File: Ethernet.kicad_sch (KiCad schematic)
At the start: 1 part, among them U1 rv1126/rv1109

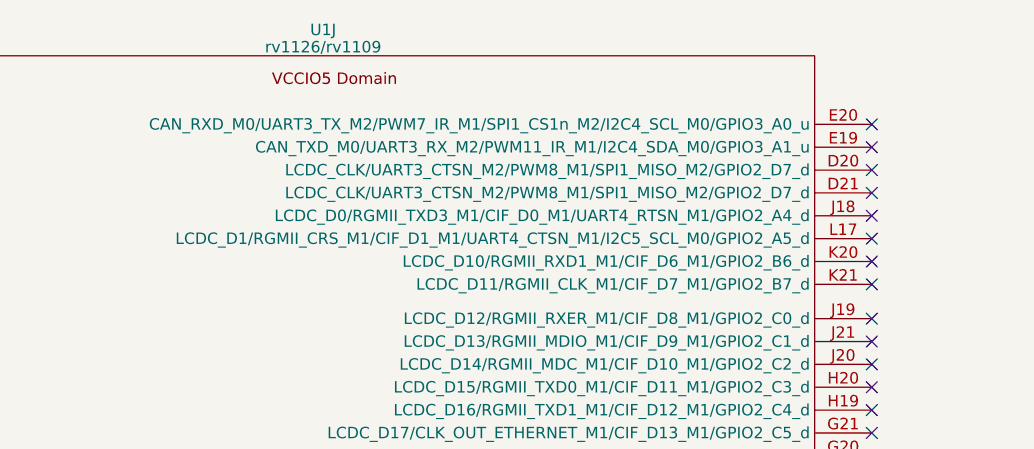
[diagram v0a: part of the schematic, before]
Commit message: fix some ERCs
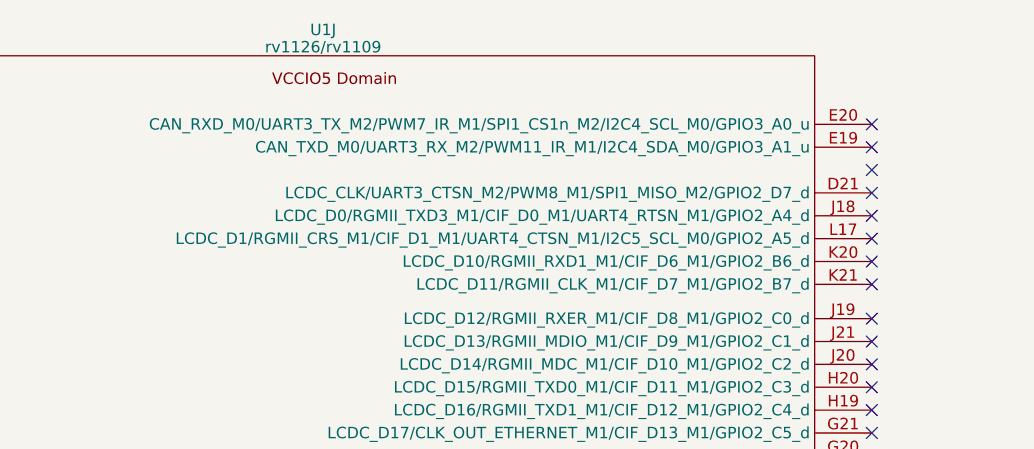
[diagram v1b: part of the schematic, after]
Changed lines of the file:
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@@
     (pin "Y21")
     (pin "C21")
-    (pin "D20")
     (pin "D21")
     (pin "E19")
@@
     (pin "Y21")
     (pin "C21")
-    (pin "D20")
     (pin "D21")
     (pin "E19")

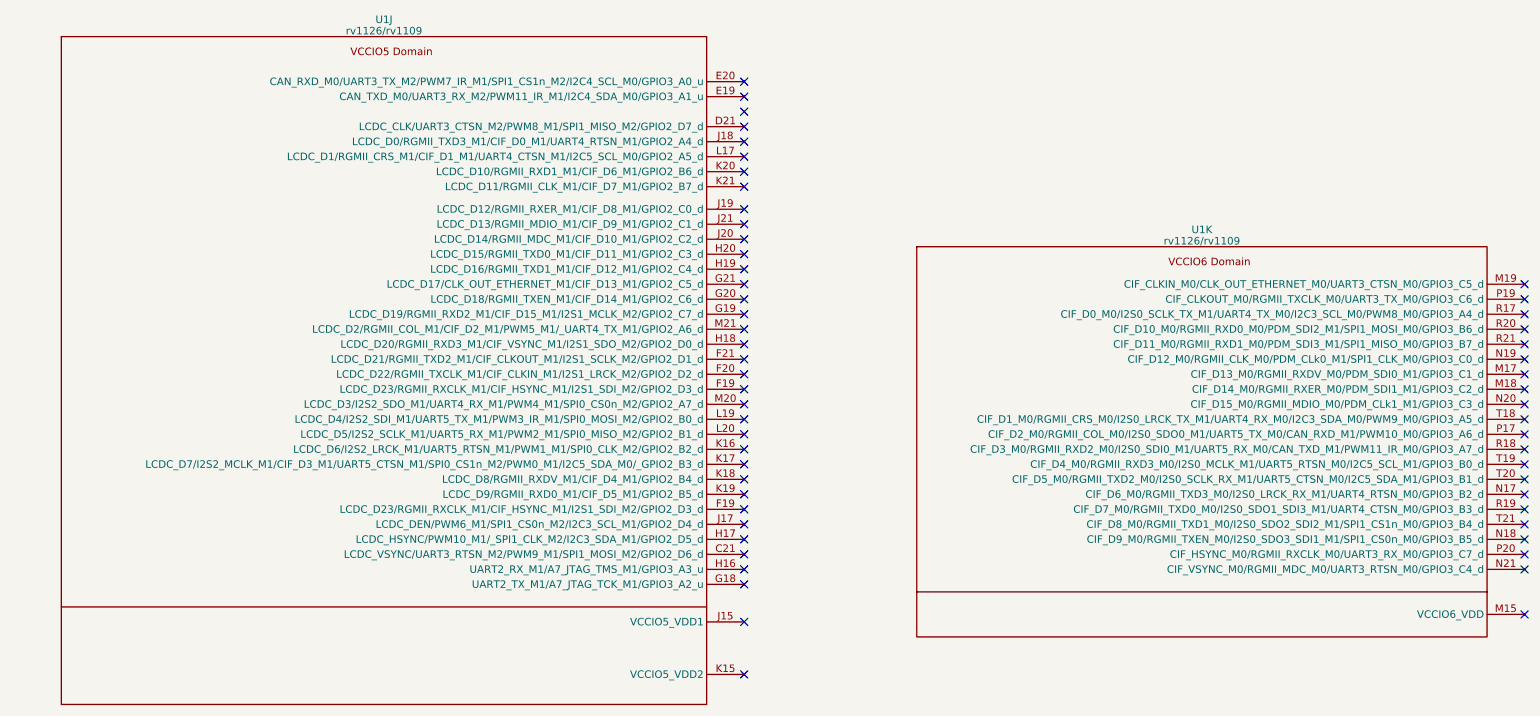
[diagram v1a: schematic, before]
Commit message: fix ERC
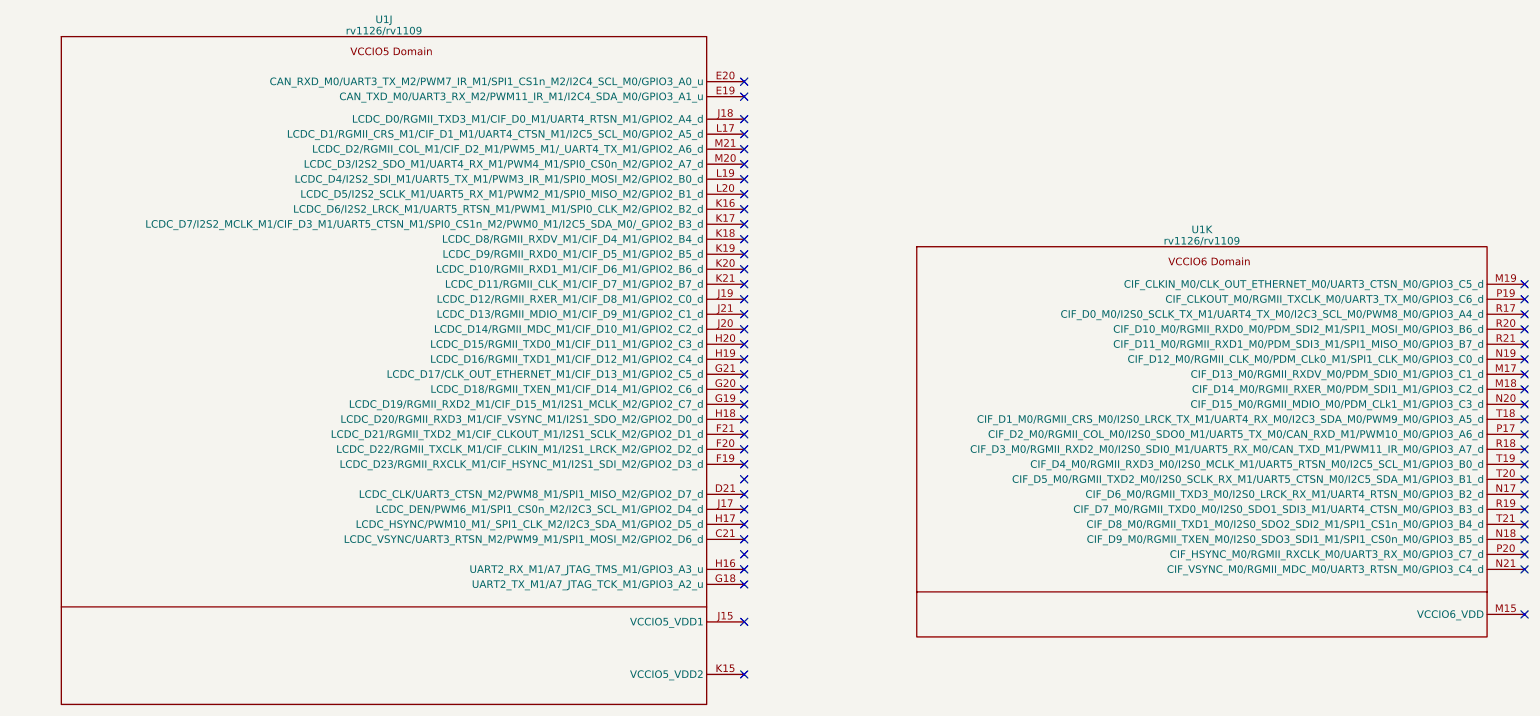
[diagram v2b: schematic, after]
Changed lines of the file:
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@@
   (no_connect (at 144.78 69.85))
   (no_connect (at 144.78 87.63))
+  (no_connect (at 144.78 41.91))
   (no_connect (at 144.78 74.93))
   (no_connect (at 276.86 80.01))
@@
   (no_connect (at 144.78 115.57))
   (no_connect (at 144.78 35.56))
-  (no_connect (at 144.78 48.26))
+  (no_connect (at 144.78 49.53))
   (no_connect (at 144.78 92.71))
   (no_connect (at 144.78 120.65))
@@
   (no_connect (at 144.78 100.33))
   (no_connect (at 276.86 125.73))
-  (no_connect (at 144.78 45.72))
-  (no_connect (at 144.78 53.34))
+  (no_connect (at 144.78 46.99))
+  (no_connect (at 144.78 54.61))
   (no_connect (at 144.78 57.15))
   (no_connect (at 144.78 90.17))
@@
   (no_connect (at 144.78 113.03))
   (no_connect (at 144.78 110.49))
-  (no_connect (at 144.78 43.18))
+  (no_connect (at 144.78 44.45))
   (no_connect (at 276.86 82.55))
   (no_connect (at 276.86 90.17))
-  (no_connect (at 144.78 50.8))
+  (no_connect (at 144.78 52.07))
   (no_connect (at 276.86 102.87))
   (no_connect (at 144.78 38.1))
   (no_connect (at 144.78 127))
-  (no_connect (at 144.78 40.64))
   (no_connect (at 276.86 105.41))
   (no_connect (at 144.78 62.23))
@@
     )
   )
-  (symbol (lib_id "CPU_Rockchip:rv1126_rv1109") (at 83.82 57.15 0) (unit 10)
+  (symbol (lib_name "rv1126_rv1109_1") (lib_id "CPU_Rockchip:rv1126_rv1109") (at 83.82 57.15 0) (unit 10)
     (in_bom yes) (on_board yes) (dnp no) (fields_autoplaced)
     (property "Reference" "U1" (at 83.82 25.0571 0)
@@
     (pin "E20")
     (pin "F19")
-    (pin "F19")
     (pin "F20")

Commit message: fix warnings
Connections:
- no-connect marks 57 -> 55
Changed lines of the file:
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@@
   (no_connect (at 144.78 107.95))
   (no_connect (at 144.78 95.25))
-  (no_connect (at 144.78 115.57))
   (no_connect (at 144.78 35.56))
   (no_connect (at 144.78 49.53))
@@
   (no_connect (at 276.86 77.47))
   (no_connect (at 276.86 69.85))
-  (no_connect (at 144.78 102.87))
   (no_connect (at 276.86 118.11))
   (no_connect (at 276.86 113.03))

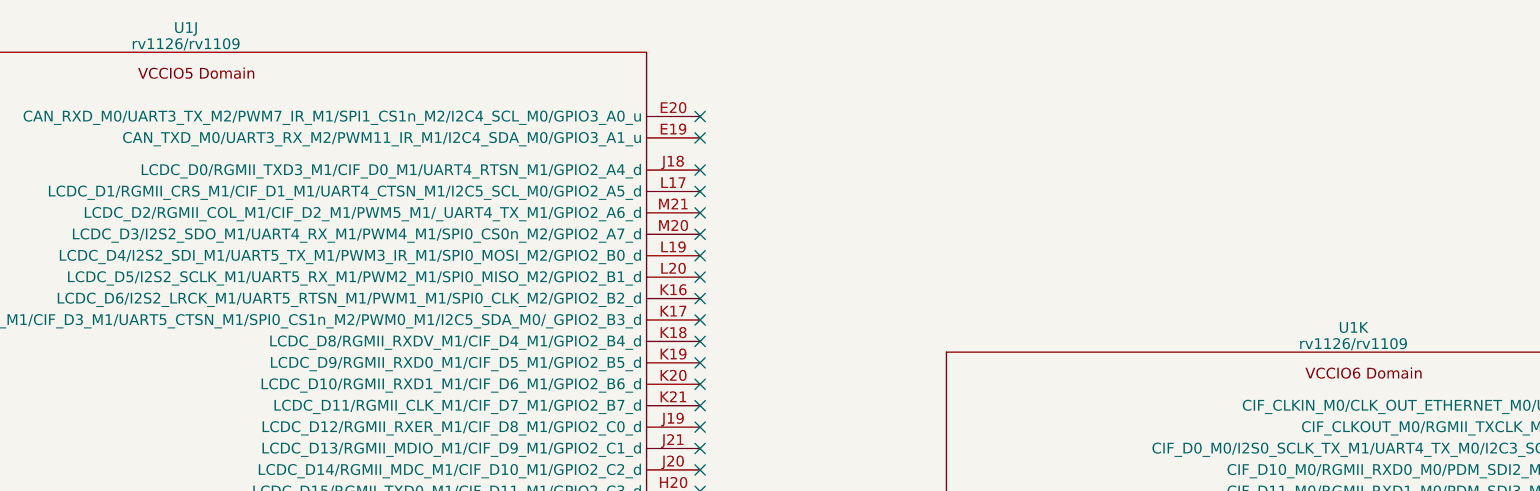
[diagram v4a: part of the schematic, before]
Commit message: added OSC, updated annotations
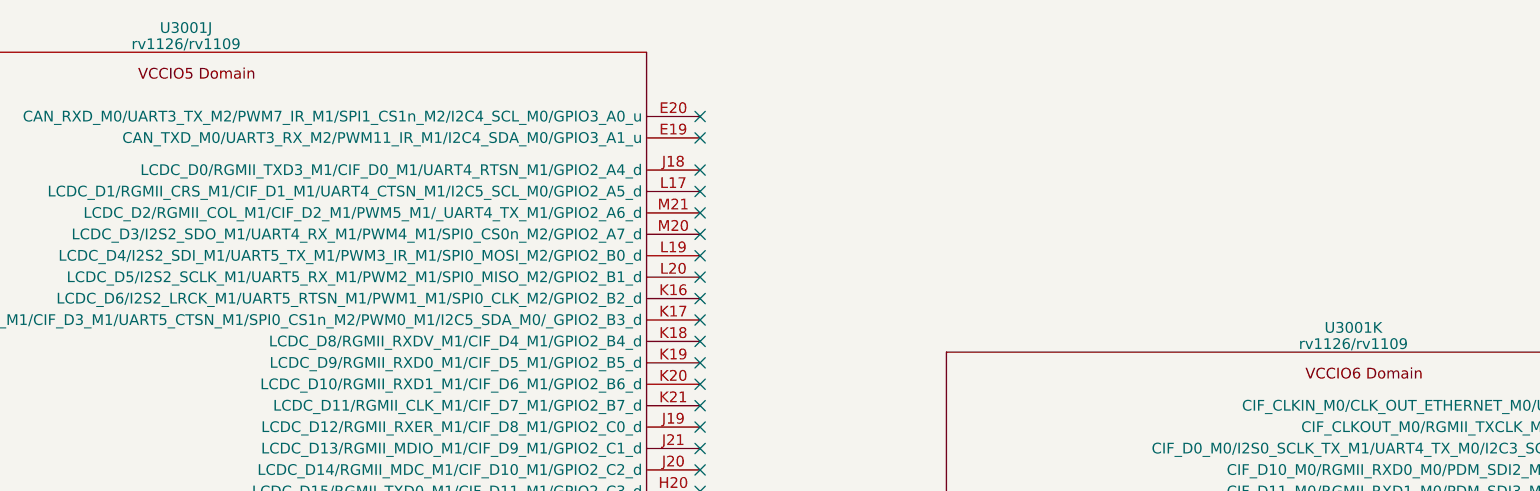
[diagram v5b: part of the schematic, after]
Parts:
- renumbered U1 to U3001
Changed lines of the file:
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@@
   (symbol (lib_id "CPU_Rockchip:rv1126_rv1109") (at 222.25 90.17 0) (unit 11)
     (in_bom yes) (on_board yes) (dnp no) (fields_autoplaced)
-    (property "Reference" "U1" (at 222.25 60.6171 0)
+    (property "Reference" "U3001" (at 222.25 60.6171 0)
       (effects (font (size 1.27 1.27)))
     )
@@
       (project "leaf"
         (path "/e3b58043-16a3-43c8-9fad-9c9784eebfa4/afbf9781-0fb6-4aca-82c1-c35bb86b79e4"
-          (reference "U1") (unit 11)
+          (reference "U3001") (unit 11)
         )
       )
@@
   (symbol (lib_id "CPU_Rockchip:rv1126_rv1109") (at 83.82 57.15 0) (unit 10)
     (in_bom yes) (on_board yes) (dnp no) (fields_autoplaced)
-    (property "Reference" "U1" (at 83.82 25.0571 0)
+    (property "Reference" "U3001" (at 83.82 25.0571 0)
       (effects (font (size 1.27 1.27)))
     )
@@
       (project "leaf"
         (path "/e3b58043-16a3-43c8-9fad-9c9784eebfa4/afbf9781-0fb6-4aca-82c1-c35bb86b79e4"
-          (reference "U1") (unit 10)
+          (reference "U3001") (unit 10)
         )
       )

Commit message: move DDR power decoupling capacitors into DDR4 Sheet
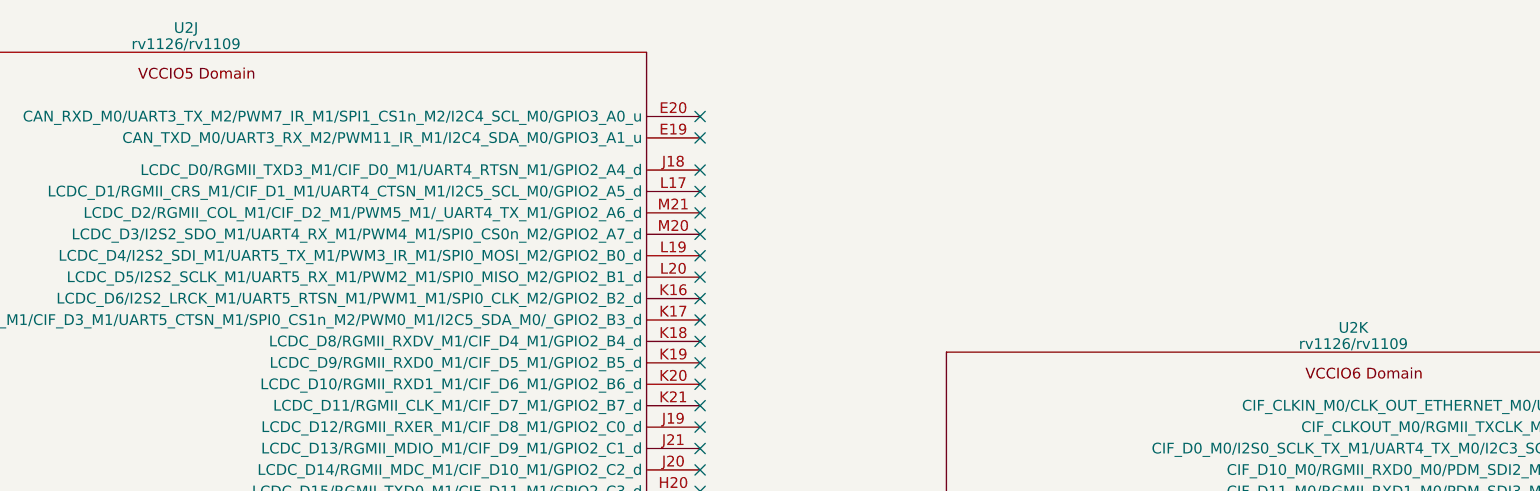
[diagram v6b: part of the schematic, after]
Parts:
- renumbered U3001 to U2
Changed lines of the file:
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@@
   (symbol (lib_id "CPU_Rockchip:rv1126_rv1109") (at 222.25 90.17 0) (unit 11)
     (in_bom yes) (on_board yes) (dnp no) (fields_autoplaced)
-    (property "Reference" "U3001" (at 222.25 60.6171 0)
+    (property "Reference" "U2" (at 222.25 60.6171 0)
       (effects (font (size 1.27 1.27)))
     )
@@
       (project "leaf"
         (path "/e3b58043-16a3-43c8-9fad-9c9784eebfa4/afbf9781-0fb6-4aca-82c1-c35bb86b79e4"
-          (reference "U3001") (unit 11)
+          (reference "U2") (unit 11)
         )
       )
@@
   (symbol (lib_id "CPU_Rockchip:rv1126_rv1109") (at 83.82 57.15 0) (unit 10)
     (in_bom yes) (on_board yes) (dnp no) (fields_autoplaced)
-    (property "Reference" "U3001" (at 83.82 25.0571 0)
+    (property "Reference" "U2" (at 83.82 25.0571 0)
       (effects (font (size 1.27 1.27)))
     )
@@
       (project "leaf"
         (path "/e3b58043-16a3-43c8-9fad-9c9784eebfa4/afbf9781-0fb6-4aca-82c1-c35bb86b79e4"
-          (reference "U3001") (unit 10)
+          (reference "U2") (unit 10)
         )
       )

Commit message: added README and license
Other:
- company: (none) -> Yang Hongbo
- title: (none) -> Leaf RV1126
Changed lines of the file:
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@@
 (kicad_sch (version 20230121) (generator eeschema)
   (paper "A4")
+  (title_block
+    (title "Leaf RV1126")
+    (date "2023-06-07")
+    (company "Yang Hongbo")
+    (comment 1 "License: CC BY-SA")
+  )
   (no_connect (at 276.86 72.39))
   (no_connect (at 144.78 69.85))
